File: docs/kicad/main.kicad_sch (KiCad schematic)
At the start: 9 parts, among them U1 ESP32-DevKitC, U2 ESP32-DevKitC, U3 ESP32-DevKitC, U4 ESP32-DevKitC

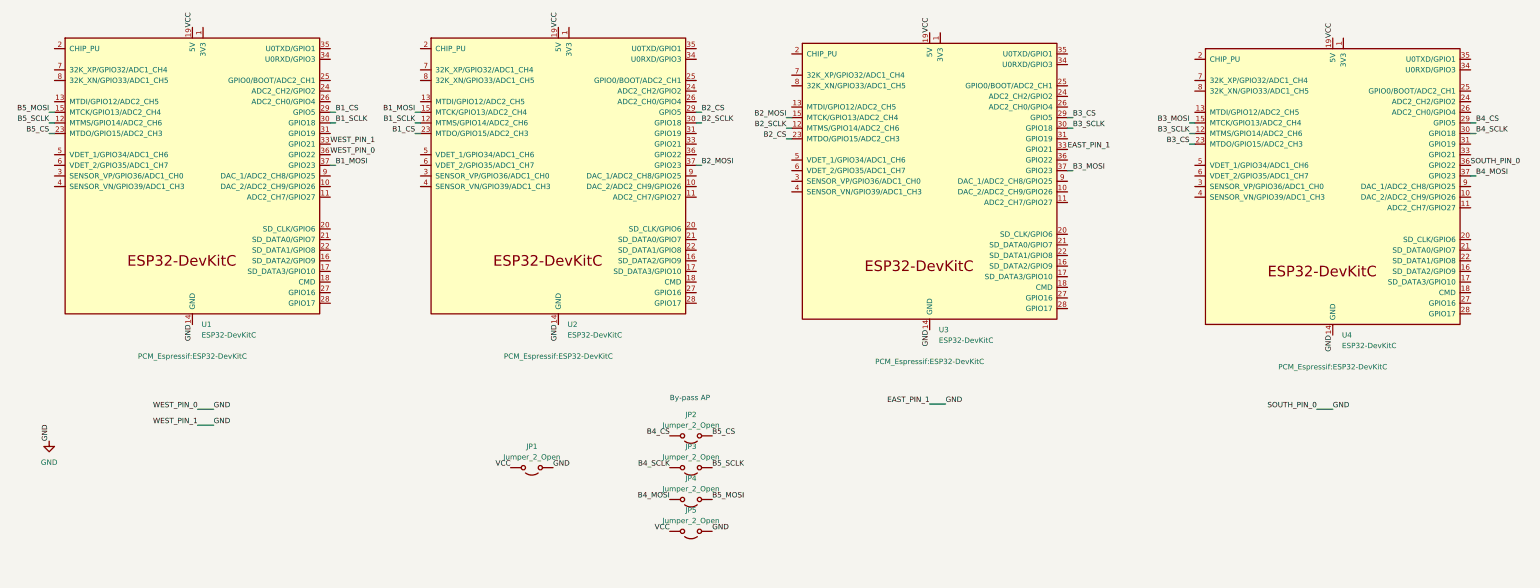
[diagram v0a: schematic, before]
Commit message: Shrink PCB + minor modifications
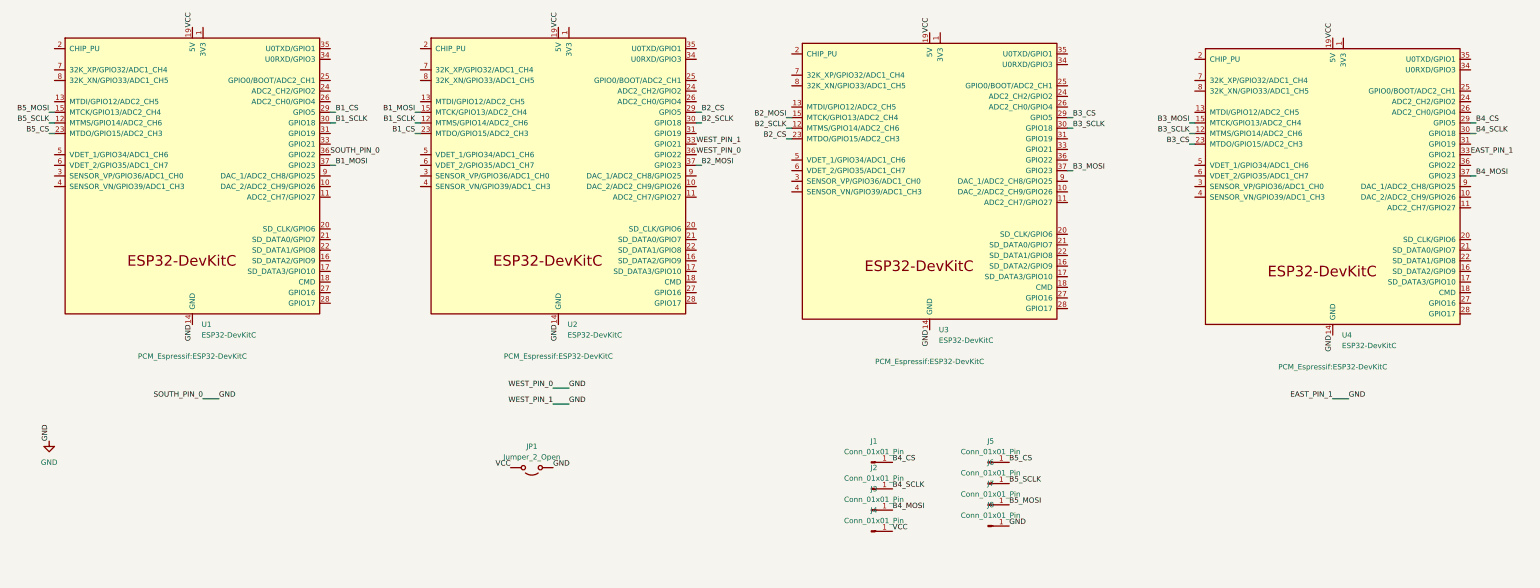
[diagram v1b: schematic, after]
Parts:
- removed JP2, JP3, JP4, JP5: Jumper_2_Open, Connector_PinSocket_1.00mm:PinSocket_1x02_P1.00mm_Vertical, symbol Jumper:Jumper_2_Open
- added J1, J2, J3, J4, J5, J6, J7, J8: Conn_01x01_Pin, Connector_PinSocket_1.27mm:PinSocket_1x01_P1.27mm_Vertical, symbol Connector:Conn_01x01_Pin
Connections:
- net B4_CS: now also J1.1 (Pin_1)
- net B4_MOSI: now also J3.1 (Pin_1)
- net B4_SCLK: now also J2.1 (Pin_1)
- net B5_CS: now also J5.1 (Pin_1)
- net B5_MOSI: now also J7.1 (Pin_1)
- net B5_SCLK: now also J6.1 (Pin_1)
- net GND: now also U2.33 (GPIO21), U2.36 (GPIO22), U4.33 (GPIO21), J8.1 (Pin_1); no longer U1.33 (GPIO21), U3.33 (GPIO21), U4.36 (GPIO22)
- net VCC: now also J4.1 (Pin_1)
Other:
- note removed: "By-pass AP"

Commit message: fixed all DRC errors/warnings
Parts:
- JP1: footprint Connector_PinSocket_1.00mm:PinSocket_1x02_P1.00mm_Vertical -> Connector_PinSocket_1.27mm:PinSocket_1x02_P1.27mm_Vertical
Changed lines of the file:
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@@
 			)
 		)
-		(property "Footprint" "Connector_PinSocket_1.00mm:PinSocket_1x02_P1.00mm_Vertical"
+		(property "Footprint" "Connector_PinSocket_1.27mm:PinSocket_1x02_P1.27mm_Vertical"
 			(at 156.2099 186.69 90)
 			(effects

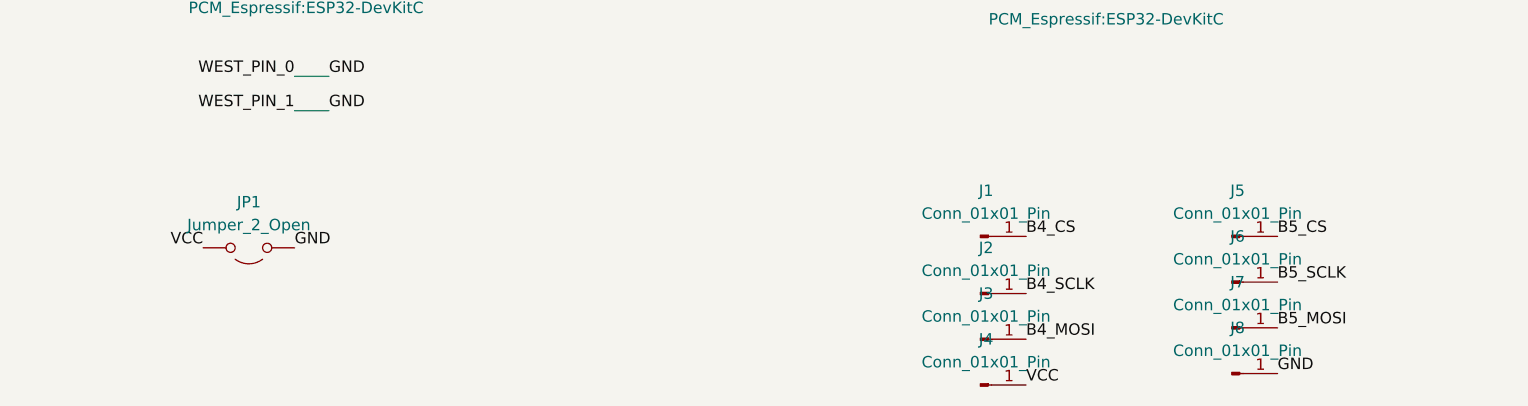
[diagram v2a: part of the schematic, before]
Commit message: used 8mm routes 1mm clearance, having some gnd islands
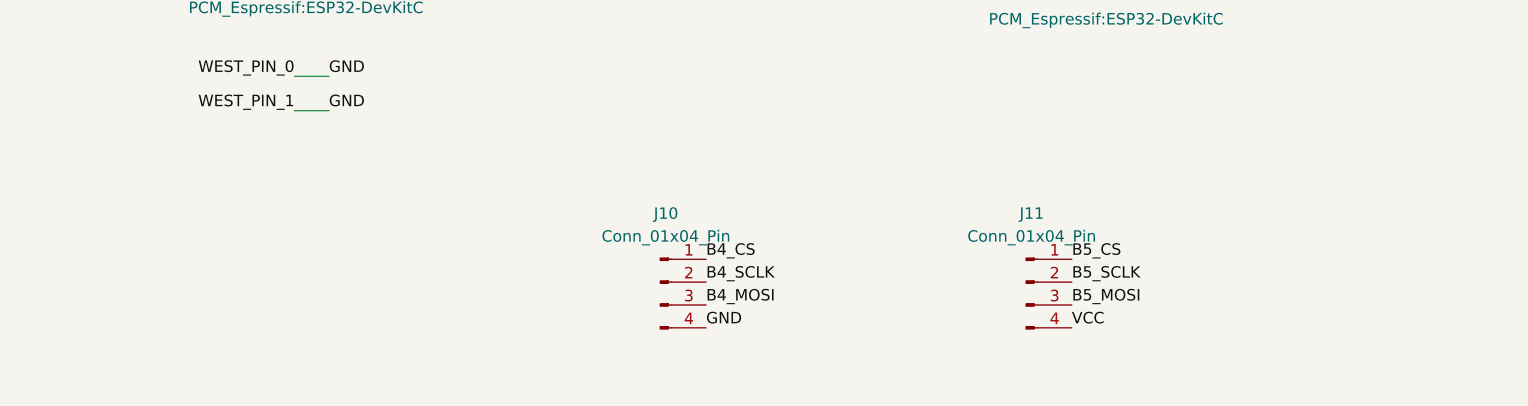
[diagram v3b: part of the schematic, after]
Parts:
- removed J1, J2, J3, J4, J5, J6, J7, J8: Conn_01x01_Pin, Connector_PinSocket_1.27mm:PinSocket_1x01_P1.27mm_Vertical, symbol Connector:Conn_01x01_Pin
- removed JP1: Jumper_2_Open, Connector_PinSocket_1.27mm:PinSocket_1x02_P1.27mm_Vertical, symbol Jumper:Jumper_2_Open
- added J10, J11: Conn_01x04_Pin, Connector_PinSocket_2.54mm:PinSocket_1x04_P2.54mm_Vertical, symbol Connector:Conn_01x04_Pin
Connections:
- net B4_CS: now also J10.1 (Pin_1)
- net B4_MOSI: now also J10.3 (Pin_3)
- net B4_SCLK: now also J10.2 (Pin_2)
- net B5_CS: now also J11.1 (Pin_1)
- net B5_MOSI: now also J11.3 (Pin_3)
- net B5_SCLK: now also J11.2 (Pin_2)
- net GND: now also J10.4 (Pin_4)
- net VCC: now also J11.4 (Pin_4)

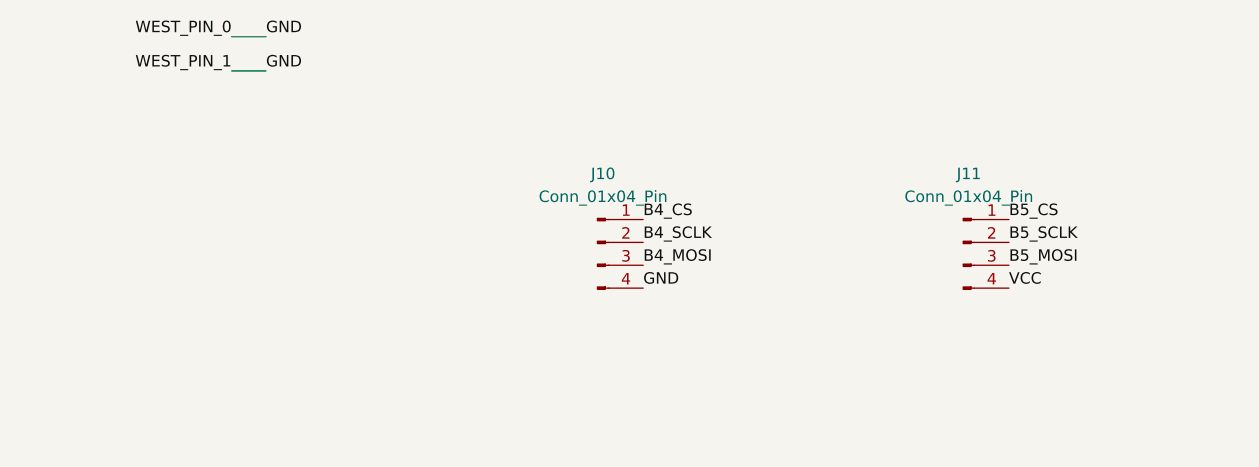
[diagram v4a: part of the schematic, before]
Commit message: use rj45 to connect
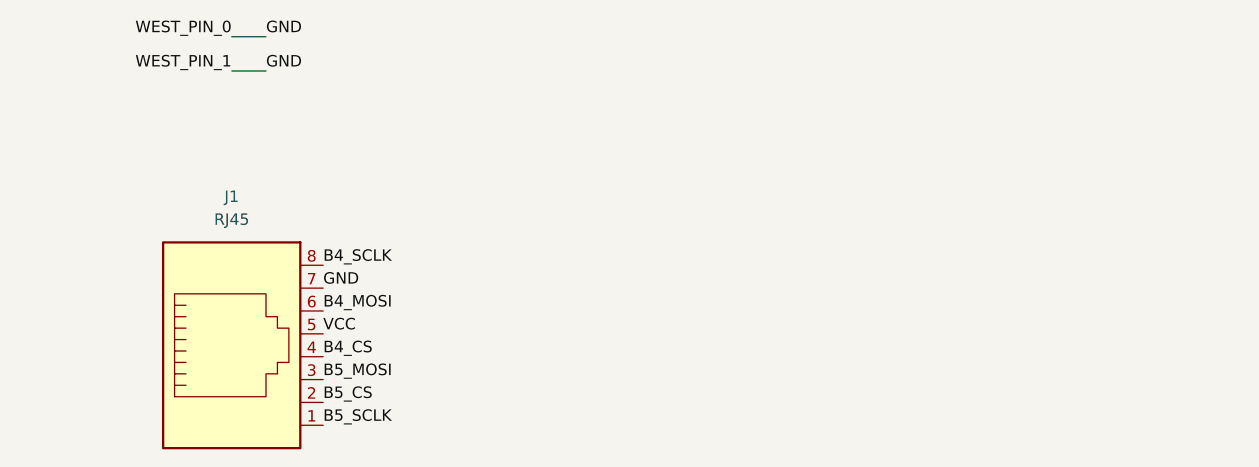
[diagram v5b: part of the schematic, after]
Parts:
- removed J10, J11: Conn_01x04_Pin, Connector_PinSocket_2.54mm:PinSocket_1x04_P2.54mm_Vertical, symbol Connector:Conn_01x04_Pin
- added J1: RJ45, Connector_RJ:RJ45_Amphenol_RJMG1BD3B8K1ANR, symbol Connector:RJ45
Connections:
- net B4_CS: now also J1.4
- net B4_MOSI: now also J1.6
- net B4_SCLK: now also J1.8
- net B5_CS: now also J1.2
- net B5_MOSI: now also J1.3
- net B5_SCLK: now also J1.1
- net GND: now also J1.7
- net VCC: now also J1.5
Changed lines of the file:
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@@
+		)
+	)
+	(label "GND"
+		(at 168.91 196.85 0)
+		(fields_autoplaced yes)
+		(effects
+			(font
+				(size 1.27 1.27)
+			)
+			(justify left bottom)
 		)
 	)
@@
 		)
 	)
+	(label "B4_MOSI"
+		(at 168.91 199.39 0)
+		(fields_autoplaced yes)
+		(effects
+			(font
+				(size 1.27 1.27)
+			)
+			(justify left bottom)
+		)
+	)
 	(label "GND"
 		(at 248.92 154.94 270)
@@
 		)
 	)
-	(label "B4_CS"
-		(at 204.47 189.23 0)
+	(label "B4_SCLK"
+		(at 168.91 194.31 0)
 		(fields_autoplaced yes)
 		(effects
@@
 		)
 	)
-	(label "B4_SCLK"
-		(at 204.47 191.77 0)
+	(label "VCC"
+		(at 168.91 201.93 0)
 		(fields_autoplaced yes)
 		(effects
@@
 		)
 	)
-	(label "VCC"
-		(at 245.11 196.85 0)
-		(fields_autoplaced yes)
-		(effects
-			(font
-				(size 1.27 1.27)
-			)
-			(justify left bottom)
-		)
-	)
 	(label "GND"
 		(at 72.39 153.67 270)
@@
 	)
 	(label "B5_SCLK"
-		(at 245.11 191.77 0)
+		(at 168.91 212.09 0)
+		(fields_autoplaced yes)
+		(effects
+			(font
+				(size 1.27 1.27)
+			)
+			(justify left bottom)
+		)
+	)
+	(label "B5_MOSI"
+		(at 168.91 207.01 0)
 		(fields_autoplaced yes)
 		(effects
@@
 		)
 	)
-	(label "B5_CS"
-		(at 245.11 189.23 0)
-		(fields_autoplaced yes)
-		(effects
-			(font
-				(size 1.27 1.27)
-			)
-			(justify left bottom)
-		)
-	)
 	(label "B2_SCLK"
 		(at 194.31 105.41 0)
@@
 		)
 	)
-	(label "GND"
-		(at 204.47 196.85 0)
-		(fields_autoplaced yes)
-		(effects
-			(font
-				(size 1.27 1.27)
-			)
-			(justify left bottom)
-		)
-	)
 	(label "B3_SCLK"
 		(at 311.15 107.95 180)
@@
 		)
 	)
+	(label "B4_CS"
+		(at 168.91 204.47 0)
+		(fields_autoplaced yes)
+		(effects
+			(font
+				(size 1.27 1.27)
+			)
+			(justify left bottom)
+		)
+	)
 	(label "B2_SCLK"
 		(at 214.63 106.68 180)
@@
 		)
 	)
-	(label "B5_MOSI"
-		(at 245.11 194.31 0)
-		(fields_autoplaced yes)
-		(effects
-			(font
-				(size 1.27 1.27)
-			)
-			(justify left bottom)
-		)
-	)
-	(label "B4_MOSI"
-		(at 204.47 194.31 0)
-		(fields_autoplaced yes)
-		(effects
-			(font
-				(size 1.27 1.27)
-			)
-			(justify left bottom)
-		)
-	)
-	(symbol
-		(lib_id "Connector:Conn_01x04_Pin")
-		(at 240.03 191.77 0)
-		(unit 1)
-		(exclude_from_sim no)
-		(in_bom yes)
-		(on_board yes)
-		(dnp no)
-		(fields_autoplaced yes)
-		(property "Reference" "J11"
-			(at 240.665 184.15 0)
-			(effects
-				(font
-					(size 1.27 1.27)
-				)
-			)
-		)
-		(property "Value" "Conn_01x04_Pin"
-			(at 240.665 186.69 0)
-			(effects
-				(font
-					(size 1.27 1.27)
-				)
-			)
-		)
-		(property "Footprint" "Connector_PinSocket_2.54mm:PinSocket_1x04_P2.54mm_Vertical"
-			(at 240.03 191.77 0)
-			(effects
-				(font
-					(size 1.27 1.27)
-				)
-				(hide yes)
-			)
-		)
-		(property "Datasheet" "~"
-			(at 240.03 191.77 0)
-			(effects
-				(font
-					(size 1.27 1.27)
-				)
-				(hide yes)
-			)
-		)
-		(property "Description" "Generic connector, single row, 01x04, script generated"
-			(at 240.03 191.77 0)
-			(effects
-				(font
-					(size 1.27 1.27)
-				)
-				(hide yes)
-			)
-		)
-		(pin "1"
-		)
-		(pin "2"
-		)
-		(pin "3"
-		)
-		(pin "4"
-		)
-		(instances
-			(project "node"
-				(path "/edfda3a5-48f3-494d-b8b7-17b5dc6cb08d/98b2ba42-50c5-4328-b2b6-bd204588fed3"
-					(reference "J11")
-					(unit 1)
-				)
-			)
+	(label "B5_CS"
+		(at 168.91 209.55 0)
+		(fields_autoplaced yes)
+		(effects
+			(font
+				(size 1.27 1.27)
+			)
+			(justify left bottom)
 		)
 	)
@@
 	)
 	(symbol
+		(lib_id "Connector:RJ45")
+		(at 158.75 204.47 0)
+		(unit 1)
+		(exclude_from_sim no)
+		(in_bom yes)
+		(on_board yes)
+		(dnp no)
+		(fields_autoplaced yes)
+		(property "Reference" "J1"
+			(at 158.75 186.69 0)
+			(effects
+				(font
+					(size 1.27 1.27)
+				)
+			)
+		)
+		(property "Value" "RJ45"
+			(at 158.75 189.23 0)
+			(effects
+				(font
+					(size 1.27 1.27)
+				)
+			)
+		)
+		(property "Footprint" "Connector_RJ:RJ45_Amphenol_RJMG1BD3B8K1ANR"
+			(at 158.75 203.835 90)
+			(effects
+				(font
+					(size 1.27 1.27)
+				)
+				(hide yes)
+			)
+		)
+		(property "Datasheet" "~"
+			(at 158.75 203.835 90)
+			(effects
+				(font
+					(size 1.27 1.27)
+				)
+				(hide yes)
+			)
+		)
+		(property "Description" "RJ connector, 8P8C (8 positions 8 connected)"
+			(at 158.75 204.47 0)
+			(effects
+				(font
+					(size 1.27 1.27)
+				)
+				(hide yes)
+			)
+		)
+		(pin "7"
+		)
+		(pin "8"
+		)
+		(pin "5"
+		)
+		(pin "6"
+		)
+		(pin "3"
+		)
+		(pin "2"
+		)
+		(pin "4"
+		)
+		(pin "1"
+		)
+		(instances
+			(project ""
+				(path "/edfda3a5-48f3-494d-b8b7-17b5dc6cb08d/98b2ba42-50c5-4328-b2b6-bd204588fed3"
+					(reference "J1")
+					(unit 1)
+				)
+			)
+		)
+	)
+	(symbol
 		(lib_id "power:GND")
 		(at 38.1 181.61 0)
@@
 					(unit 1)
 				)
-			)
-		)
-	)
-	(symbol
-		(lib_id "Connector:Conn_01x04_Pin")
-		(at 199.39 191.77 0)
-		(unit 1)
-		(exclude_from_sim no)
-		(in_bom yes)
-		(on_board yes)
-		(dnp no)
-		(fields_autoplaced yes)
-		(property "Reference" "J10"
-			(at 200.025 184.15 0)
-			(effects
-				(font
-					(size 1.27 1.27)
-				)
-			)
-		)
-		(property "Value" "Conn_01x04_Pin"
-			(at 200.025 186.69 0)
-			(effects
-				(font
-					(size 1.27 1.27)
-				)
-			)
-		)
-		(property "Footprint" "Connector_PinSocket_2.54mm:PinSocket_1x04_P2.54mm_Vertical"
-			(at 199.39 191.77 0)
-			(effects
-				(font
-					(size 1.27 1.27)
-				)
-				(hide yes)
-			)
-		)
-		(property "Datasheet" "~"
-			(at 199.39 191.77 0)
-			(effects
-				(font
-					(size 1.27 1.27)
-				)
-				(hide yes)
-			)
-		)
-		(property "Description" "Generic connector, single row, 01x04, script generated"
-			(at 199.39 191.77 0)
-			(effects
-				(font
-					(size 1.27 1.27)
-				)
-				(hide yes)
-			)
-		)
-		(pin "1"
-		)
-		(pin "2"
-		)
-		(pin "3"
-		)
-		(pin "4"
-		)
-		(instances
-			(project ""
-				(path "/edfda3a5-48f3-494d-b8b7-17b5dc6cb08d/98b2ba42-50c5-4328-b2b6-bd204588fed3"
-					(reference "J10")
-					(unit 1)
-				)
